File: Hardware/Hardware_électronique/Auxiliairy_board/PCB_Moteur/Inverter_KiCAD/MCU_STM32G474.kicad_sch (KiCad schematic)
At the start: 45 parts, among them J801 USB_C_Receptacle_USB2.0, J802 Conn_01x05, J803 Conn_ST_STDC14, J804 Conn_01x04, SW801 SW_Push, SW802 SW_Push, SW803 SW_Push, SW804 SW_Push, SW805 SW_Push, U801 STM32G474RETx, U802 USBLC6-2SC6, Y801 16M

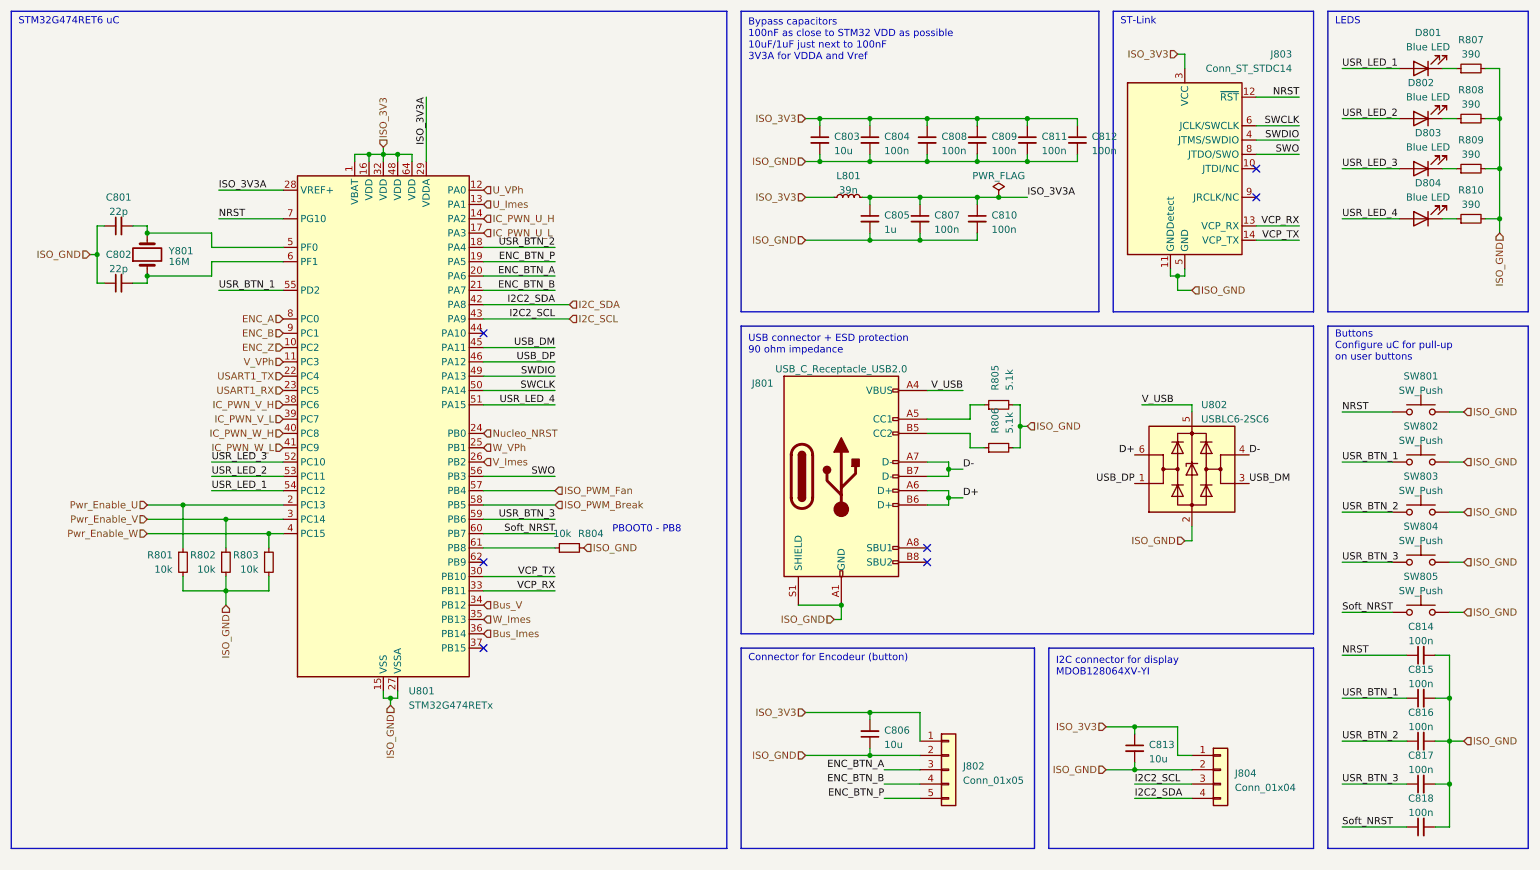
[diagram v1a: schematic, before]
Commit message: update schematic
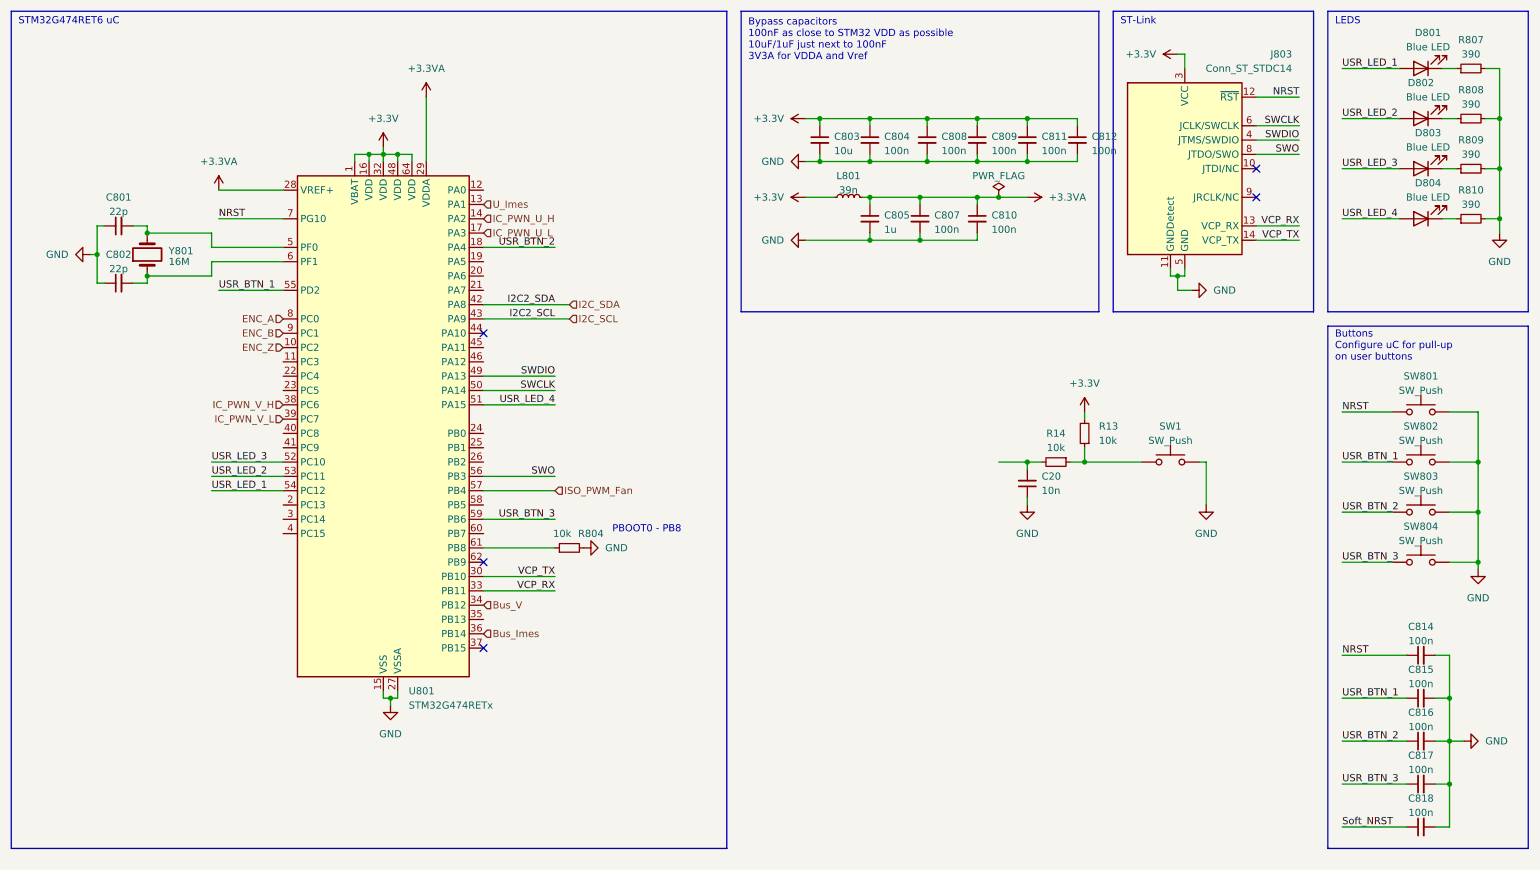
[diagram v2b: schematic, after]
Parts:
- removed C806, C813: 10u, Capacitor_SMD:C_0603_1608Metric, symbol Device:C_Small
- removed J801: USB_C_Receptacle_USB2.0, Connector_USB:USB_C_Receptacle_HRO_TYPE-C-31-M-12, symbol Connector:USB_C_Receptacle_USB2.0
- removed J802: Conn_01x05, Connector_JST:JST_XH_B5B-XH-A_1x05_P2.50mm_Vertical, symbol Connector_Generic:Conn_01x05
- removed J804: Conn_01x04, Connector_JST:JST_XH_B4B-XH-A_1x04_P2.50mm_Vertical, symbol Connector_Generic:Conn_01x04
- removed R801, R802, R803: 10k, Resistor_SMD:R_0402_1005Metric, symbol Device:R_Small
- removed R805, R806: 5.1k, Resistor_SMD:R_0402_1005Metric, symbol Device:R_Small
- removed SW805: SW_Push, Custom:435451019820, symbol Switch:SW_Push
- removed U802: USBLC6-2SC6, Package_TO_SOT_SMD:SOT-23-6, symbol Power_Protection:USBLC6-2SC6
- added C20: 10n, Capacitor_SMD:C_0402_1005Metric, symbol Device:C_Small
- added R13, R14: 10k, symbol Device:R_Small
- added SW1: SW_Push, Custom:435451019820, symbol Switch:SW_Push
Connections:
- net Soft_NRST: no longer U801.60 (PB7)
- net ENC_BTN_A: no longer names the net of U801.20 (PA6)
- net ENC_BTN_B: no longer names the net of U801.21 (PA7)
- net ENC_BTN_P: no longer names the net of U801.19 (PA5)
- net IC_PWN_W_H: no longer names the net of U801.40 (PC8)
- net IC_PWN_W_L: no longer names the net of U801.41 (PC9)
- net ISO_3V3 renamed +3.3V
- net +3.3V: now also R13.2
- net ISO_3V3A renamed +3.3VA
- net ISO_GND renamed GND
- net GND: now also C20.1, SW1.2
- net ISO_PWM_Break: no longer names the net of U801.58 (PB5)
- net Nucleo_NRST: no longer names the net of U801.24 (PB0)
- net Pwr_Enable_U: no longer names the net of U801.2 (PC13)
- net Pwr_Enable_V: no longer names the net of U801.3 (PC14)
- net Pwr_Enable_W: no longer names the net of U801.4 (PC15)
- net USART1_RX: no longer names the net of U801.23 (PC5)
- net USART1_TX: no longer names the net of U801.22 (PC4)
- net USB_DM: no longer names the net of U801.45 (PA11)
- net USB_DP: no longer names the net of U801.46 (PA12)
- net U_VPh: no longer names the net of U801.12 (PA0)
- net V_Imes: no longer names the net of U801.26 (PB2)
- net V_VPh: no longer names the net of U801.11 (PC3)
- net W_Imes: no longer names the net of U801.35 (PB13)
- net W_VPh: no longer names the net of U801.25 (PB1)
- new net: R13.1, R14.1, SW1.1
- new net: C20.2, R14.2
- no-connect marks 7 -> 5
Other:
- note removed: "Connector for Encodeur (button)"
- note removed: "I2C connector for display MDOB128064XV-YI"
- note removed: "USB connector + ESD protection 90 ohm impedance"

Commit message: update schematic
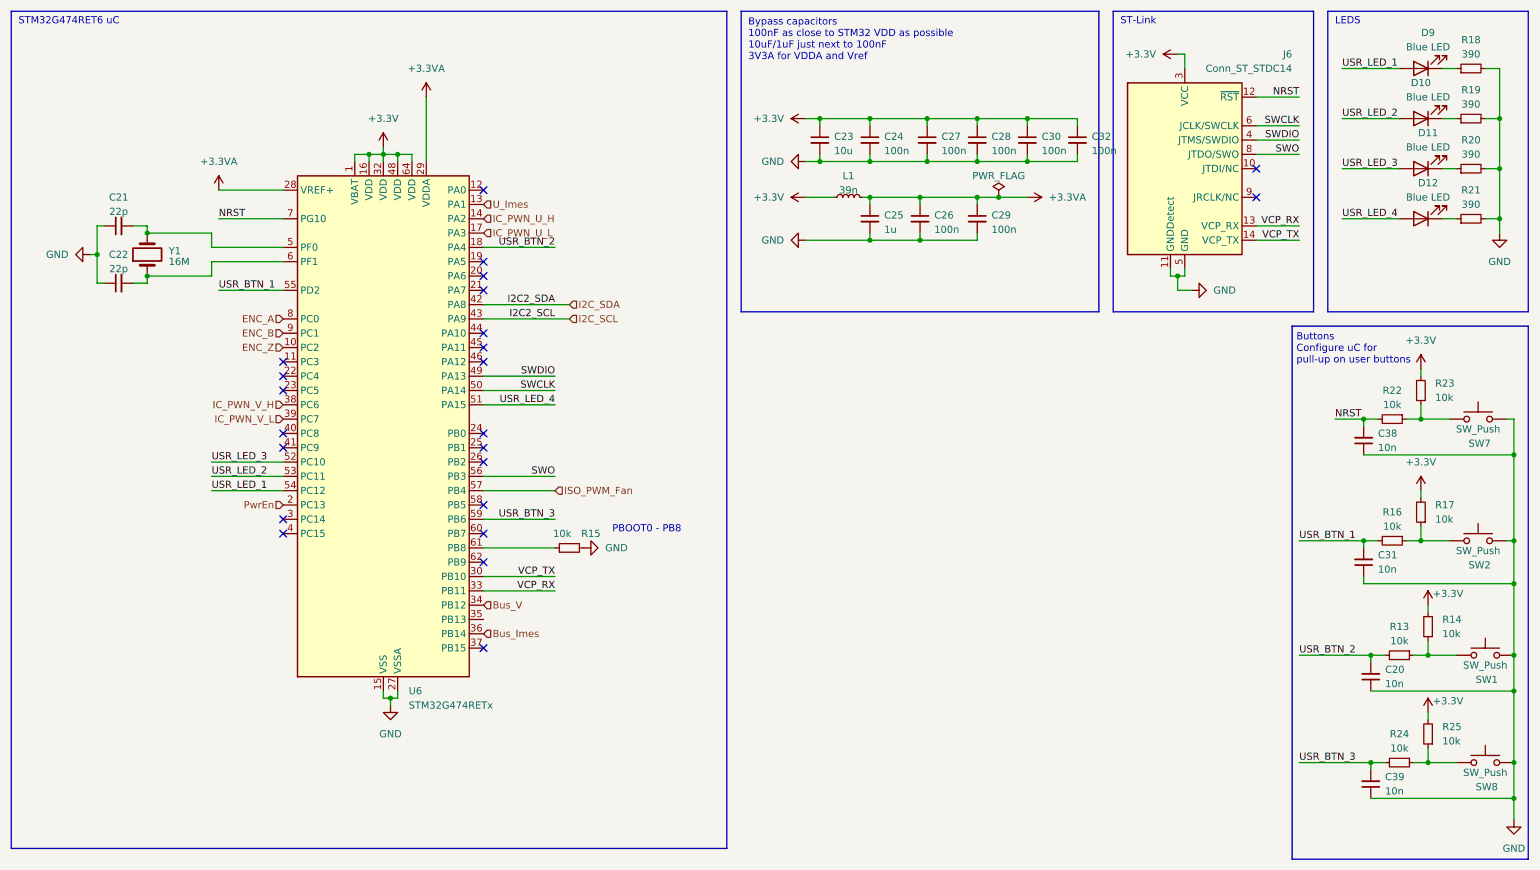
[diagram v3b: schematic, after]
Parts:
- removed C814, C815, C816, C817, C818: 100n, Capacitor_SMD:C_0402_1005Metric, symbol Device:C_Small
- removed SW801, SW802, SW803, SW804: SW_Push, Custom:435451019820, symbol Switch:SW_Push
- added C20, C38, C39: 10n, Capacitor_SMD:C_0402_1005Metric, symbol Device:C_Small
- added R13, R14, R22, R23, R24, R25: 10k, symbol Device:R_Small
- added SW1, SW7, SW8: SW_Push, Custom:435451019820, symbol Switch:SW_Push
- renumbered C801 to C21, C802 to C22, C803 to C23, C804 to C24, C805 to C25, C807 to C26, C808 to C27, C809 to C28, C810 to C29, C811 to C30, C20 to C31, C812 to C32, D802 to D10, D803 to D11, D804 to D12, D801 to D9, J803 to J6, L801 to L1, R804 to R15, R14 to R16, R13 to R17, R807 to R18, R808 to R19, R809 to R20, R810 to R21, SW1 to SW2, U801 to U6, Y801 to Y1
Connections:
- net +3.3V: now also R14.2, R23.2, R25.2
- net GND: now also C20.1, C38.1, C39.1, SW1.2, SW7.2, SW8.2
- net NRST: now also C38.2, R22.2
- net USR_BTN_1: now also C31.2, R16.2
- net USR_BTN_2: now also C20.2, R13.2
- net USR_BTN_3: now also C39.2, R24.2
- net PwrEn: now reaches U6.2 (PC13)
- new net: R24.1, R25.1, SW8.1
- new net: R22.1, R23.1, SW7.1
- new net: R13.1, R14.1, SW1.1
- no-connect marks 5 -> 23
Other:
- moved on the sheet: C31, R16, R17, SW2

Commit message: last schematic editing
just miss a  FB resistor value
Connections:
- no-connect marks 23 -> 24
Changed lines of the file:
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@@
 	)
 	(no_connect
+		(at 97.79 121.92)
+	)
+	(no_connect
 		(at 97.79 88.9)
 	)
@@
 		)
 	)
-	(label "I2C2_SCL"
-		(at 110.49 68.58 180)
-		(fields_autoplaced yes)
-		(effects
-			(font
-				(size 1.27 1.27)
-			)
-			(justify right bottom)
-		)
-	)
 	(label "SWO"
 		(at 110.49 96.52 180)
@@
 		)
 	)
-	(label "I2C2_SDA"
-		(at 110.49 66.04 180)
-		(fields_autoplaced yes)
-		(effects
-			(font
-				(size 1.27 1.27)
-			)
-			(justify right bottom)
-		)
-	)
 	(label "SWCLK"
 		(at 110.49 81.28 180)
@@
 		(on_board yes)
 		(dnp no)
-		(fields_autoplaced yes)
 		(property "Reference" "C32"
-			(at 205.74 36.2013 0)
+			(at 199.39 29.21 0)
 			(effects
 				(font
@@
 		)
 		(property "Value" "100n"
-			(at 205.74 38.7413 0)
+			(at 199.136 30.988 0)
 			(effects
 				(font

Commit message: almost finished pcb
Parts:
- C23: footprint Capacitor_SMD:C_0603_1608Metric -> Capacitor_SMD:C_0603_1608Metric_Pad1.08x0.95mm_HandSolder
- C25: footprint Capacitor_SMD:C_0402_1005Metric -> Capacitor_SMD:C_0603_1608Metric_Pad1.08x0.95mm_HandSolder
- R13, R14, R16, R17, R22, R23, R24, R25: footprint (none) -> Resistor_SMD:R_0402_1005Metric
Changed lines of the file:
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@@
 			)
 		)
-		(property "Footprint" ""
+		(property "Footprint" "Resistor_SMD:R_0402_1005Metric"
 			(at 265.43 142.24 0)
 			(effects
@@
 			)
 		)
-		(property "Footprint" ""
+		(property "Footprint" "Resistor_SMD:R_0402_1005Metric"
 			(at 264.16 81.28 0)
 			(effects
@@
 			)
 		)
-		(property "Footprint" "Capacitor_SMD:C_0603_1608Metric"
+		(property "Footprint" "Capacitor_SMD:C_0603_1608Metric_Pad1.08x0.95mm_HandSolder"
 			(at 157.48 36.83 0)
 			(effects
@@
 			)
 		)
-		(property "Footprint" ""
+		(property "Footprint" "Resistor_SMD:R_0402_1005Metric"
 			(at 265.43 123.19 0)
 			(effects
@@
 			)
 		)
-		(property "Footprint" ""
+		(property "Footprint" "Resistor_SMD:R_0402_1005Metric"
 			(at 264.16 102.87 0)
 			(effects
@@
 			)
 		)
-		(property "Footprint" ""
+		(property "Footprint" "Resistor_SMD:R_0402_1005Metric"
 			(at 259.08 86.36 0)
 			(effects
@@
 			)
 		)
-		(property "Footprint" "Capacitor_SMD:C_0402_1005Metric"
+		(property "Footprint" "Capacitor_SMD:C_0603_1608Metric_Pad1.08x0.95mm_HandSolder"
 			(at 166.37 50.8 0)
 			(effects
@@
 			)
 		)
-		(property "Footprint" ""
+		(property "Footprint" "Resistor_SMD:R_0402_1005Metric"
 			(at 259.08 107.95 0)
 			(effects
@@
 			)
 		)
-		(property "Footprint" ""
+		(property "Footprint" "Resistor_SMD:R_0402_1005Metric"
 			(at 260.35 128.27 0)
 			(effects
@@
 			)
 		)
-		(property "Footprint" ""
+		(property "Footprint" "Resistor_SMD:R_0402_1005Metric"
 			(at 260.35 147.32 0)
 			(effects

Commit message: finalization
Rooting and last edits ready to go
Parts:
- added J7: Conn_01x02, Connector_JST:JST_XH_B2B-XH-A_1x02_P2.50mm_Vertical, symbol Connector_Generic:Conn_01x02
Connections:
- net USART1_RX: now reaches U6.22 (PC4)
- net USART1_RX: now also J7.1 (Pin_1)
- net USART1_TX: now reaches U6.23 (PC5)
- net USART1_TX: now also J7.2 (Pin_2)
- no-connect marks 24 -> 22
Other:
- note added: "UART To Mother Board"
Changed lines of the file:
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@@
 	)
 	(no_connect
-		(at 62.23 76.2)
-	)
-	(no_connect
 		(at 97.79 63.5)
 	)
@@
 	)
 	(no_connect
-		(at 62.23 81.28)
-	)
-	(no_connect
-		(at 62.23 78.74)
+		(at 62.23 76.2)
 	)
 	(no_connect
@@
 	(wire
 		(pts
+			(xy 154.94 83.82) (xy 170.18 83.82)
+		)
+		(stroke
+			(width 0)
+			(type default)
+		)
+	)
+	(wire
+		(pts
 			(xy 261.62 107.95) (xy 264.16 107.95)
 		)
@@
 	(wire
 		(pts
+			(xy 154.94 81.28) (xy 170.18 81.28)
+		)
+		(stroke
+			(width 0)
+			(type default)
+		)
+	)
+	(wire
+		(pts
 			(xy 81.28 135.89) (xy 81.28 137.16)
 		)
@@
 	(wire
 		(pts
+			(xy 46.99 81.28) (xy 62.23 81.28)
+		)
+		(stroke
+			(width 0)
+			(type default)
+		)
+	)
+	(wire
+		(pts
 			(xy 255.27 128.27) (xy 257.81 128.27)
 		)
@@
 	(wire
 		(pts
+			(xy 46.99 78.74) (xy 62.23 78.74)
+		)
+		(stroke
+			(width 0)
+			(type default)
+		)
+	)
+	(wire
+		(pts
 			(xy 82.55 39.37) (xy 82.55 40.64)
 		)
@@
 	)
 	(rectangle
+		(start 153.035 73.66)
+		(end 193.675 90.805)
+		(stroke
+			(width 0)
+			(type default)
+		)
+		(fill
+			(type none)
+		)
+	)
+	(rectangle
 		(start 143.51 13.97)
 		(end 207.01 67.31)
@@
 		)
 	)
+	(text "UART To Mother Board"
+		(exclude_from_sim no)
+		(at 164.338 75.184 0)
+		(effects
+			(font
+				(size 1.27 1.27)
+			)
+		)
+	)
 	(text "PBOOT0 - PB8\n"
 		(exclude_from_sim no)
@@
 		)
 	)
+	(label "USART1_TX"
+		(at 154.94 83.82 0)
+		(fields_autoplaced yes)
+		(effects
+			(font
+				(size 1.27 1.27)
+			)
+			(justify left bottom)
+		)
+	)
 	(label "USR_LED_1"
 		(at 49.53 99.06 0)
@@
 		)
 	)
+	(label "USART1_TX"
+		(at 46.99 81.28 0)
+		(fields_autoplaced yes)
+		(effects
+			(font
+				(size 1.27 1.27)
+			)
+			(justify left bottom)
+		)
+	)
 	(label "SWDIO"
 		(at 242.57 36.83 180)
@@
 		)
 	)
+	(label "USART1_RX"
+		(at 46.99 78.74 0)
+		(fields_autoplaced yes)
+		(effects
+			(font
+				(size 1.27 1.27)
+			)
+			(justify left bottom)
+		)
+	)
 	(label "VCP_RX"
 		(at 242.57 52.07 180)
@@
 		)
 	)
+	(label "USART1_RX"
+		(at 154.94 81.28 0)
+		(fields_autoplaced yes)
+		(effects
+			(font
+				(size 1.27 1.27)
+			)
+			(justify left bottom)
+		)
+	)
 	(label "USR_LED_2"
 		(at 49.53 96.52 0)
@@
 					(unit 1)
 				)
+			)
+		)
+	)
+	(symbol
+		(lib_id "Connector_Generic:Conn_01x02")
+		(at 175.26 81.28 0)
+		(unit 1)
+		(exclude_from_sim no)
+		(in_bom yes)
+		(on_board yes)
+		(dnp no)
+		(fields_autoplaced yes)
+		(property "Reference" "J7"
+			(at 177.8 81.2799 0)
+			(effects
+				(font
+					(size 1.27 1.27)
+				)
+				(justify left)
+			)
+		)
+		(property "Value" "Conn_01x02"
+			(at 177.8 83.8199 0)
+			(effects
+				(font
+					(size 1.27 1.27)
+				)
+				(justify left)
+			)
+		)
+		(property "Footprint" "Connector_JST:JST_XH_B2B-XH-A_1x02_P2.50mm_Vertical"
+			(at 175.26 81.28 0)
+			(effects
+				(font
+					(size 1.27 1.27)
+				)
+				(hide yes)
+			)
+		)
+		(property "Datasheet" "~"
+			(at 175.26 81.28 0)
+			(effects
+				(font
+					(size 1.27 1.27)
+				)
+				(hide yes)
+			)
+		)
+		(property "Description" "Generic connector, single row, 01x02, script generated (kicad-library-utils/schlib/autogen/connector/)"
+			(at 175.26 81.28 0)
+			(effects
+				(font
+					(size 1.27 1.27)
+				)
+				(hide yes)
+			)
+		)
+		(pin "1"
+		)
+		(pin "2"
+		)
+		(instances
+			(project "Inverter_KiCAD"
+				(path "/5e6c1e3f-0815-454a-8acb-8e3e2d064875/fbaaf7ce-bae7-41f7-a7d1-9e6954b2dbcf"
+					(reference "J7")
+					(unit 1)
+				)
